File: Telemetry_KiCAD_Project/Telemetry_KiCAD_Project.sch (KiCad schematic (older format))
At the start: 1 part, among them J1 50Ω SMA Connector

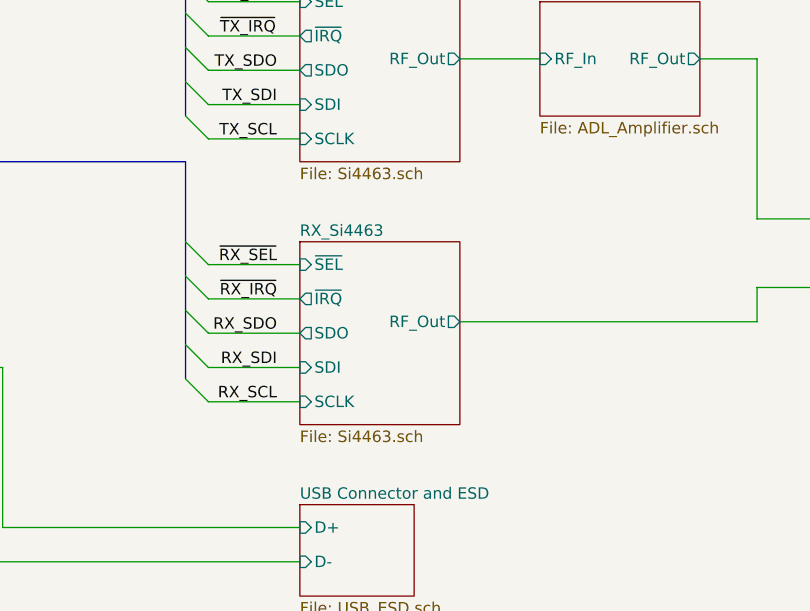
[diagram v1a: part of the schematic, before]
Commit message: Created separate schematics for chips acting in TX and RX
Added link to document describing passive component selection
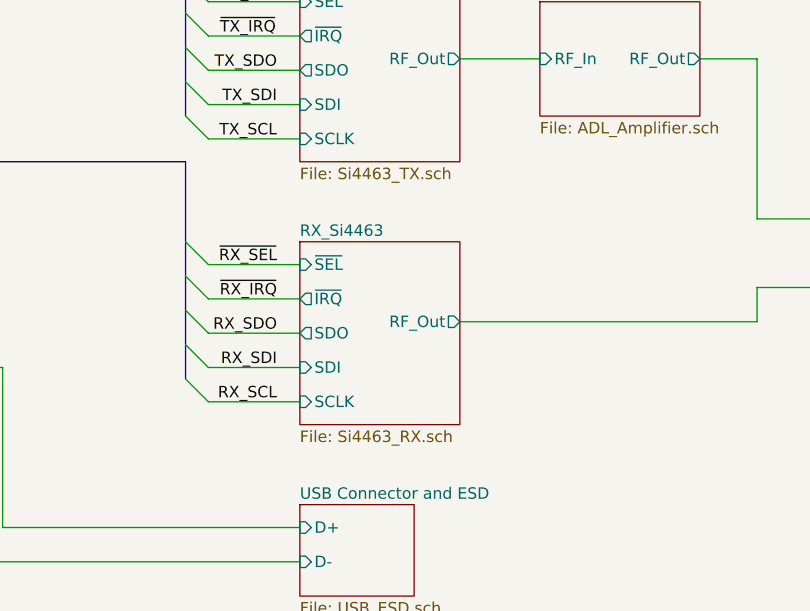
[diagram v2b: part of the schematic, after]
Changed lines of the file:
@@
 	8050 3450 7700 3450
-$Sheet
-S 4900 2250 700  800
-U 619D9C89
-F0 "TX_Si4463" 50
-F1 "Si4463.sch" 50
-F2 "~SEL" I L 4900 2350 50
-F3 "SDI" I L 4900 2800 50
-F4 "SCLK" I L 4900 2950 50
-F5 "~IRQ" O L 4900 2500 50
-F6 "SDO" O L 4900 2650 50
-F7 "RF_Out" O R 5600 2600 50
-$EndSheet
 $Sheet
 S 5950 2350 700  500
@@
 F2 "RF_In" I L 5950 2600 50
 F3 "RF_Out" O R 6650 2600 50
-$EndSheet
-$Sheet
-S 4900 3400 700  800
-U 61A0416A
-F0 "RX_Si4463" 50
-F1 "Si4463.sch" 50
-F2 "~SEL" I L 4900 3500 50
-F3 "SDI" I L 4900 3950 50
-F4 "SCLK" I L 4900 4100 50
-F5 "~IRQ" O L 4900 3650 50
-F6 "SDO" O L 4900 3800 50
-F7 "RF_Out" O R 5600 3750 50
 $EndSheet
 Wire Wire Line
@@
 Wire Bus Line
 	4400 3050 4400 4000
+$Sheet
+S 4900 3400 700  800
+U 61A0416A
+F0 "RX_Si4463" 50
+F1 "Si4463_RX.sch" 50
+F2 "~SEL" I L 4900 3500 50
+F3 "SDI" I L 4900 3950 50
+F4 "SCLK" I L 4900 4100 50
+F5 "~IRQ" O L 4900 3650 50
+F6 "SDO" O L 4900 3800 50
+F7 "RF_Out" O R 5600 3750 50
+$EndSheet
+$Sheet
+S 4900 2250 700  800
+U 619D9C89
+F0 "TX_Si4463" 50
+F1 "Si4463_TX.sch" 50
+F2 "~SEL" I L 4900 2350 50
+F3 "SDI" I L 4900 2800 50
+F4 "SCLK" I L 4900 2950 50
+F5 "~IRQ" O L 4900 2500 50
+F6 "SDO" O L 4900 2650 50
+F7 "RF_Out" O R 5600 2600 50
+$EndSheet
 $EndSCHEMATC
